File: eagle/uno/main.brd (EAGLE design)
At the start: 35.9 x 39.4 mm, 10 parts

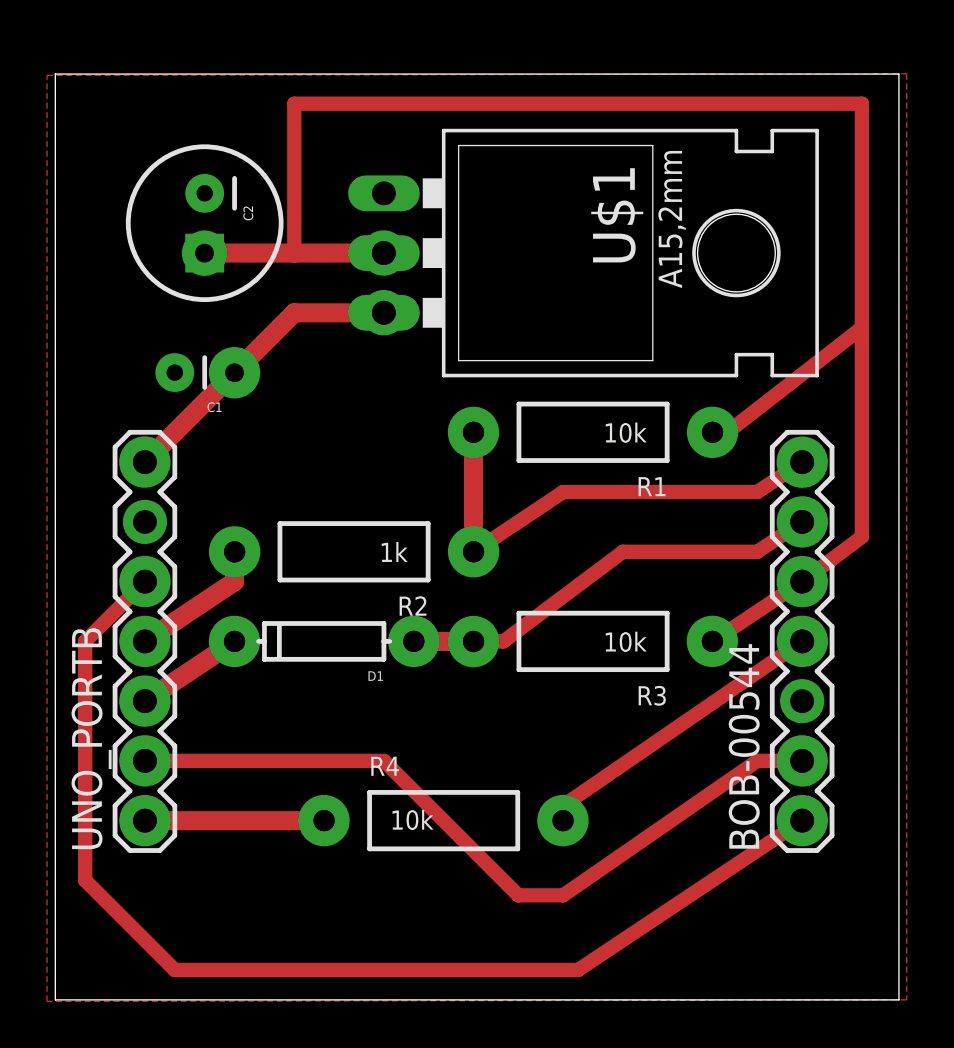
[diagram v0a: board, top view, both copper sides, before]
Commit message: [ fix ] eagle/uno, voltage regulator footprint (TO220)
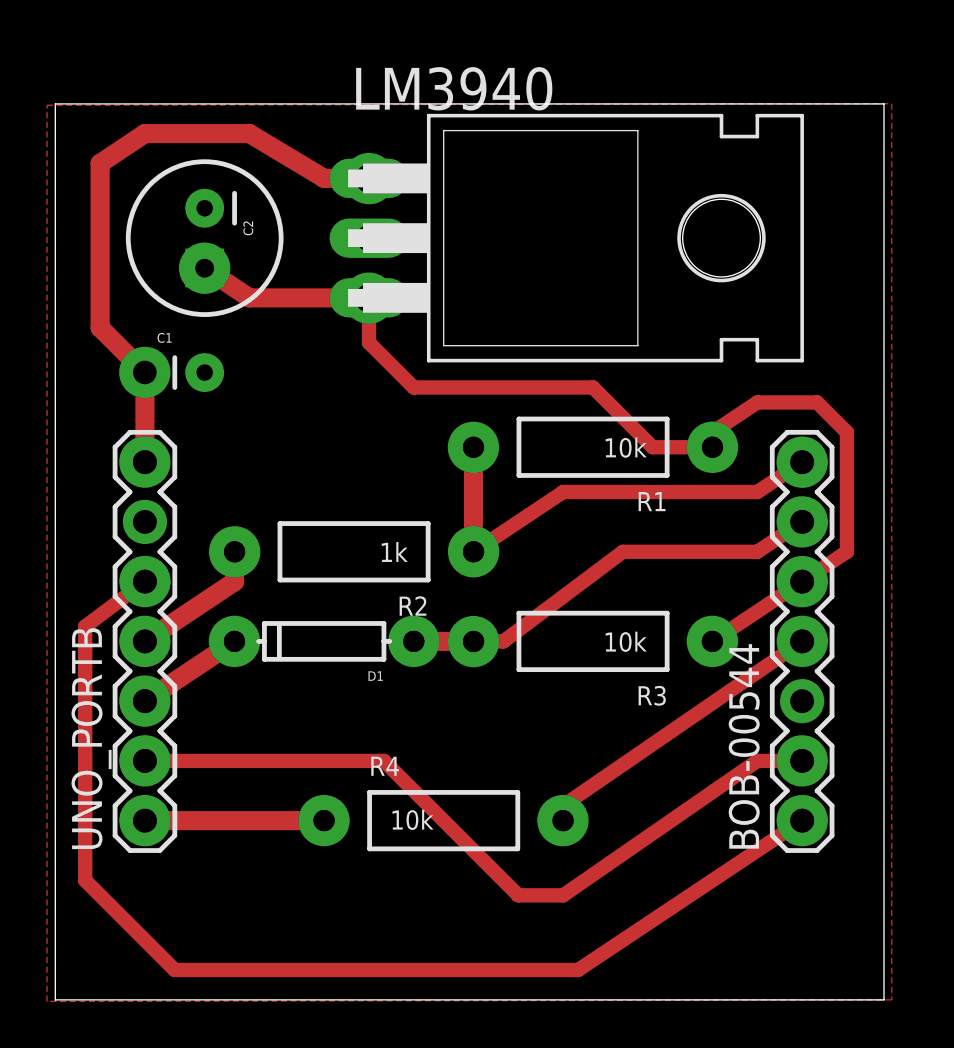
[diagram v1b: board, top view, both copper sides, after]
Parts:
- removed U$1: V_REG_LD1117VXX, SparkFun:78XXL
- added LM3940: LM340H-05, linear:TO220H
- moved C1 3.81 mm to (2.54, 21.6), turned to 0 degrees
- moved C2 0.64 mm to (5.08, 27.3)
- moved R1 0.64 mm to (21.6, 18.4)
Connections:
- net 3.3V: now also LM3940.3; no longer U$1.GND
- net 5V: now also LM3940.1; no longer U$1.OUT
- net GND: now also LM3940.2; no longer U$1.IN
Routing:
- net 3.3V: track 72.1 -> 44.9 mm
- net 5V: track 12.8 -> 25.8 mm
- net CS: track 20.2 -> 19.6 mm
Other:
- board size 35.9 x 39.4 mm -> 35.2 x 38.1 mm
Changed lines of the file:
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@@
 <setting verticaltext="up"/>
 </settings>
-<grid distance="0.635" unitdist="mm" unit="mm" style="lines" multiple="1" display="yes" altdistance="0.025" altunitdist="inch" altunit="inch"/>
+<grid distance="0.1" unitdist="inch" unit="inch" style="lines" multiple="1" display="yes" altdistance="0.025" altunitdist="inch" altunit="inch"/>
 <layers>
 <layer number="1" name="Top" color="4" fill="1" visible="yes" active="yes"/>
@@
 <board>
 <plain>
-<wire x1="-1.27" y1="-5.08" x2="34.595" y2="-5.08" width="0" layer="20"/>
-<wire x1="34.595" y1="-5.08" x2="34.595" y2="34.28" width="0" layer="20"/>
-<wire x1="34.595" y1="34.28" x2="-1.27" y2="34.28" width="0" layer="20"/>
-<wire x1="-1.27" y1="34.28" x2="-1.27" y2="-5.08" width="0" layer="20"/>
+<wire x1="-1.27" y1="-5.08" x2="33.96" y2="-5.08" width="0" layer="20"/>
+<wire x1="33.96" y1="-5.08" x2="33.96" y2="33.01" width="0" layer="20"/>
+<wire x1="33.96" y1="33.01" x2="-1.27" y2="33.01" width="0" layer="20"/>
+<wire x1="-1.27" y1="33.01" x2="-1.27" y2="-5.08" width="0" layer="20"/>
 </plain>
 <attributes>
@@
 <element name="BOB-00544" library="SparkFun" package="1X07" value="" x="30.48" y="2.54" rot="R90"/>
 <element name="UNO_PORTB" library="SparkFun" package="1X07" value="" x="2.54" y="2.54" rot="R90"/>
-<element name="R1" library="SparkFun" package="AXIAL-0.4" value="10k" x="21.59" y="19.05" rot="R180"/>
+<element name="R1" library="SparkFun" package="AXIAL-0.4" value="10k" x="21.59" y="18.415" rot="R180"/>
 <element name="R2" library="SparkFun" package="AXIAL-0.4" value="1k" x="11.43" y="13.97" rot="R180"/>
 <element name="R3" library="SparkFun" package="AXIAL-0.4" value="10k" x="21.59" y="10.16" rot="R180"/>
 <element name="R4" library="SparkFun" package="AXIAL-0.4" value="10k" x="15.24" y="2.54"/>
 <element name="D1" library="SparkFun" package="DIODE-1N4148" value="" x="10.16" y="10.16" rot="R180"/>
-<element name="C1" library="SparkFun" package="CAP-PTH-SMALL" value="10nf" x="6.35" y="21.59" rot="R180"/>
-<element name="C2" library="SparkFun" package="CPOL-RADIAL-100UF-25V" value="35uf" x="5.08" y="27.94" rot="R270"/>
-<element name="U$1" library="SparkFun" package="78XXL" value="V_REG_LD1117VXX" x="16.51" y="26.67" rot="R270"/>
+<element name="C1" library="SparkFun" package="CAP-PTH-SMALL" value="10nf" x="2.54" y="21.59"/>
+<element name="C2" library="SparkFun" package="CPOL-RADIAL-100UF-25V" value="35uf" x="5.08" y="27.305" rot="R270"/>
+<element name="LM3940" library="linear" package="TO220H" value="LM340H-05" x="22.225" y="27.305" rot="R270"/>
 </elements>
 <signals>
@@
 <contactref element="R1" pad="P$2"/>
 <contactref element="R2" pad="P$1"/>
-<wire x1="16.51" y1="19.05" x2="16.51" y2="13.97" width="0.8128" layer="1"/>
+<wire x1="16.51" y1="18.415" x2="16.51" y2="13.97" width="0.8128" layer="1"/>
 <wire x1="30.48" y1="17.78" x2="28.575" y2="16.51" width="0.6096" layer="1"/>
 <wire x1="28.575" y1="16.51" x2="20.32" y2="16.51" width="0.6096" layer="1"/>
@@
 <signal name="GND">
 <contactref element="BOB-00544" pad="3"/>
-<contactref element="U$1" pad="IN"/>
 <contactref element="C2" pad="2"/>
 <contactref element="C1" pad="2"/>
 <contactref element="UNO_PORTB" pad="6"/>
 <polygon width="0.3048" layer="1" isolate="0.4064">
-<vertex x="-1.622171875" y="34.22394375"/>
-<vertex x="34.925" y="34.29"/>
-<vertex x="34.925" y="-5.08"/>
+<vertex x="-1.622171875" y="32.95394375"/>
+<vertex x="34.29" y="33.02"/>
+<vertex x="34.29" y="-5.08"/>
 <vertex x="-1.622171875" y="-5.14605625"/>
 </polygon>
+<contactref element="LM3940" pad="2"/>
 </signal>
 <signal name="CD">
 <contactref element="BOB-00544" pad="1"/>
 <contactref element="UNO_PORTB" pad="5"/>
-<wire x1="2.54" y1="12.7" x2="0" y2="10.16" width="0.6096" layer="1"/>
-<wire x1="0" y1="10.16" x2="0" y2="0" width="0.6096" layer="1"/>
+<wire x1="2.54" y1="12.7" x2="0" y2="10.795" width="0.6096" layer="1"/>
+<wire x1="0" y1="10.795" x2="0" y2="0" width="0.6096" layer="1"/>
 <wire x1="0" y1="0" x2="3.81" y2="-3.81" width="0.6096" layer="1"/>
 <wire x1="3.81" y1="-3.81" x2="20.955" y2="-3.81" width="0.6096" layer="1"/>
@@
 </signal>
 <signal name="5V">
-<contactref element="U$1" pad="OUT"/>
 <contactref element="C1" pad="1"/>
-<wire x1="12.7" y1="24.13" x2="8.89" y2="24.13" width="0.8128" layer="1"/>
-<wire x1="8.89" y1="24.13" x2="6.35" y2="21.59" width="0.8128" layer="1"/>
 <contactref element="UNO_PORTB" pad="7"/>
-<wire x1="6.35" y1="21.59" x2="2.54" y2="17.78" width="0.8128" layer="1"/>
+<contactref element="LM3940" pad="1"/>
+<wire x1="12.065" y1="29.845" x2="10.16" y2="29.845" width="0.8128" layer="1"/>
+<wire x1="10.16" y1="29.845" x2="6.985" y2="31.75" width="0.8128" layer="1"/>
+<wire x1="6.985" y1="31.75" x2="2.54" y2="31.75" width="0.8128" layer="1"/>
+<wire x1="2.54" y1="31.75" x2="0.635" y2="30.48" width="0.8128" layer="1"/>
+<wire x1="0.635" y1="30.48" x2="0.635" y2="23.495" width="0.8128" layer="1"/>
+<wire x1="0.635" y1="23.495" x2="2.54" y2="21.59" width="0.8128" layer="1"/>
+<wire x1="2.54" y1="17.78" x2="2.54" y2="21.59" width="0.8128" layer="1"/>
 </signal>
 <signal name="3.3V">
-<contactref element="U$1" pad="GND"/>
 <contactref element="C2" pad="1"/>
 <contactref element="R1" pad="P$1"/>
 <contactref element="R3" pad="P$1"/>
 <contactref element="BOB-00544" pad="5"/>
-<wire x1="5.08" y1="26.67" x2="8.89" y2="26.67" width="0.8128" layer="1"/>
-<wire x1="8.89" y1="26.67" x2="12.7" y2="26.67" width="0.8128" layer="1"/>
-<wire x1="26.67" y1="19.05" x2="27.305" y2="19.05" width="0.6096" layer="1"/>
-<wire x1="27.305" y1="19.05" x2="33.02" y2="23.495" width="0.6096" layer="1"/>
-<wire x1="33.02" y1="23.495" x2="33.02" y2="33.02" width="0.6096" layer="1"/>
-<wire x1="33.02" y1="33.02" x2="8.89" y2="33.02" width="0.6096" layer="1"/>
-<wire x1="8.89" y1="33.02" x2="8.89" y2="26.67" width="0.6096" layer="1"/>
-<wire x1="30.48" y1="12.7" x2="33.02" y2="14.605" width="0.6096" layer="1"/>
-<wire x1="33.02" y1="14.605" x2="33.02" y2="23.495" width="0.6096" layer="1"/>
-<wire x1="26.67" y1="10.16" x2="30.48" y2="12.7" width="0.6096" layer="1"/>
-</signal>
-<signal name="N$3">
-<via x="6.349896875" y="21.58225" extent="1-16" drill="0.8" diameter="2.1844"/>
+<contactref element="LM3940" pad="3"/>
+<wire x1="5.08" y1="26.035" x2="6.985" y2="24.765" width="0.8128" layer="1"/>
+<wire x1="6.985" y1="24.765" x2="12.065" y2="24.765" width="0.8128" layer="1"/>
+<wire x1="30.48" y1="12.7" x2="32.385" y2="13.97" width="0.6096" layer="1"/>
+<wire x1="32.385" y1="13.97" x2="32.385" y2="19.05" width="0.6096" layer="1"/>
+<wire x1="32.385" y1="19.05" x2="31.115" y2="20.32" width="0.6096" layer="1"/>
+<wire x1="12.065" y1="24.765" x2="12.065" y2="22.86" width="0.6096" layer="1"/>
+<wire x1="30.48" y1="12.7" x2="26.67" y2="10.16" width="0.6096" layer="1"/>
+<wire x1="12.065" y1="22.86" x2="13.97" y2="20.955" width="0.6096" layer="1"/>
+<wire x1="13.97" y1="20.955" x2="21.59" y2="20.955" width="0.6096" layer="1"/>
+<wire x1="21.59" y1="20.955" x2="24.13" y2="18.415" width="0.6096" layer="1"/>
+<wire x1="24.13" y1="18.415" x2="26.67" y2="18.415" width="0.6096" layer="1"/>
+<wire x1="26.67" y1="18.415" x2="26.67" y2="19.05" width="0.6096" layer="1"/>
+<wire x1="26.67" y1="19.05" x2="28.575" y2="20.32" width="0.6096" layer="1"/>
+<wire x1="28.575" y1="20.32" x2="31.115" y2="20.32" width="0.6096" layer="1"/>
 </signal>
 <signal name="N$4">
-<via x="16.50618125" y="19.0456375" extent="1-16" drill="0.9" diameter="2.1844"/>
+<via x="16.50618125" y="18.4106375" extent="1-16" drill="0.9" diameter="2.1844"/>
 </signal>
 <signal name="N$5">
@@
 </signal>
 <signal name="N$13">
-<via x="26.66975" y="19.048596875" extent="1-16" drill="0.9" diameter="2.1844"/>
+<via x="26.66975" y="18.413596875" extent="1-16" drill="0.9" diameter="2.1844"/>
 </signal>
 <signal name="N$14">
 <via x="2.536909375" y="17.78494375" extent="1-16" drill="1" diameter="2.1844"/>
+<via x="2.536909375" y="21.59494375" extent="1-16" drill="1" diameter="2.1844"/>
+<wire x1="2.536909375" y1="17.78494375" x2="2.536909375" y2="21.59494375" width="0" layer="19" extent="1-1"/>
 </signal>
 <signal name="N$16">
@@
 <via x="30.484975" y="2.541446875" extent="1-16" drill="1" diameter="2.1844"/>
 </signal>
-<signal name="N$28">
-<via x="5.07381875" y="26.66463125" extent="1-16" drill="0.8" diameter="1.9304" shape="square"/>
-</signal>
-<signal name="N$30">
-<via x="12.68854375" y="26.672190625" extent="1-16" drill="1" diameter="1.9304" shape="square"/>
-</signal>
-<signal name="N$31">
-<via x="12.696278125" y="24.134903125" extent="1-16" drill="1" diameter="1.9304" shape="square"/>
+<signal name="N$2">
+<via x="5.079515625" y="26.02535625" extent="1-16" drill="0.8" diameter="2.1844" shape="square"/>
+</signal>
+<signal name="N$1">
+<via x="12.067140625" y="29.835309375" extent="1-16" drill="1.2" diameter="2.1844" shape="square"/>
+</signal>
+<signal name="N$3">
+<via x="12.060778125" y="24.752490625" extent="1-16" drill="1.2" diameter="2.1844" shape="square"/>
 </signal>
 </signals>
